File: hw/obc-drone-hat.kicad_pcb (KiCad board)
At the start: 4 copper layers, 65 x 56.5 mm, 68 parts, among them SW1 SW_DIP_x04

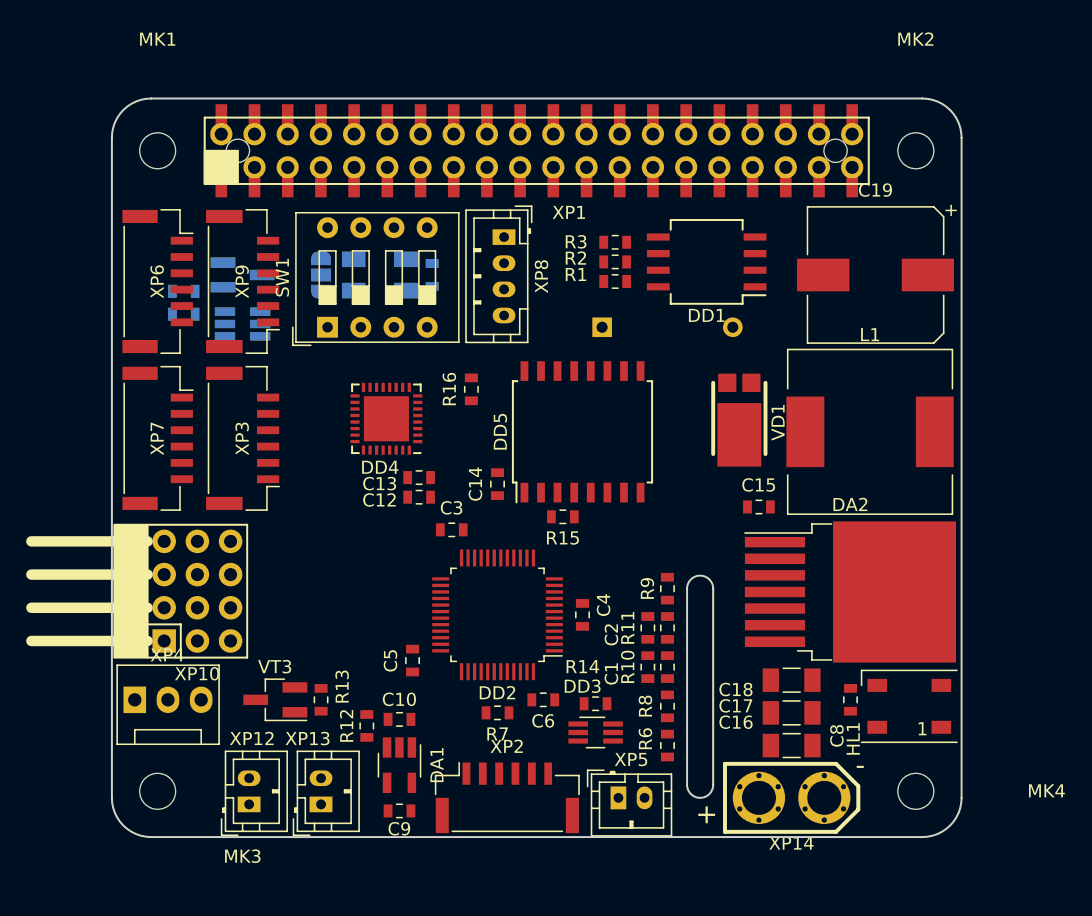
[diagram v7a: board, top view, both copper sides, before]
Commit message: hw: prepare to start wiring. add global GND planes
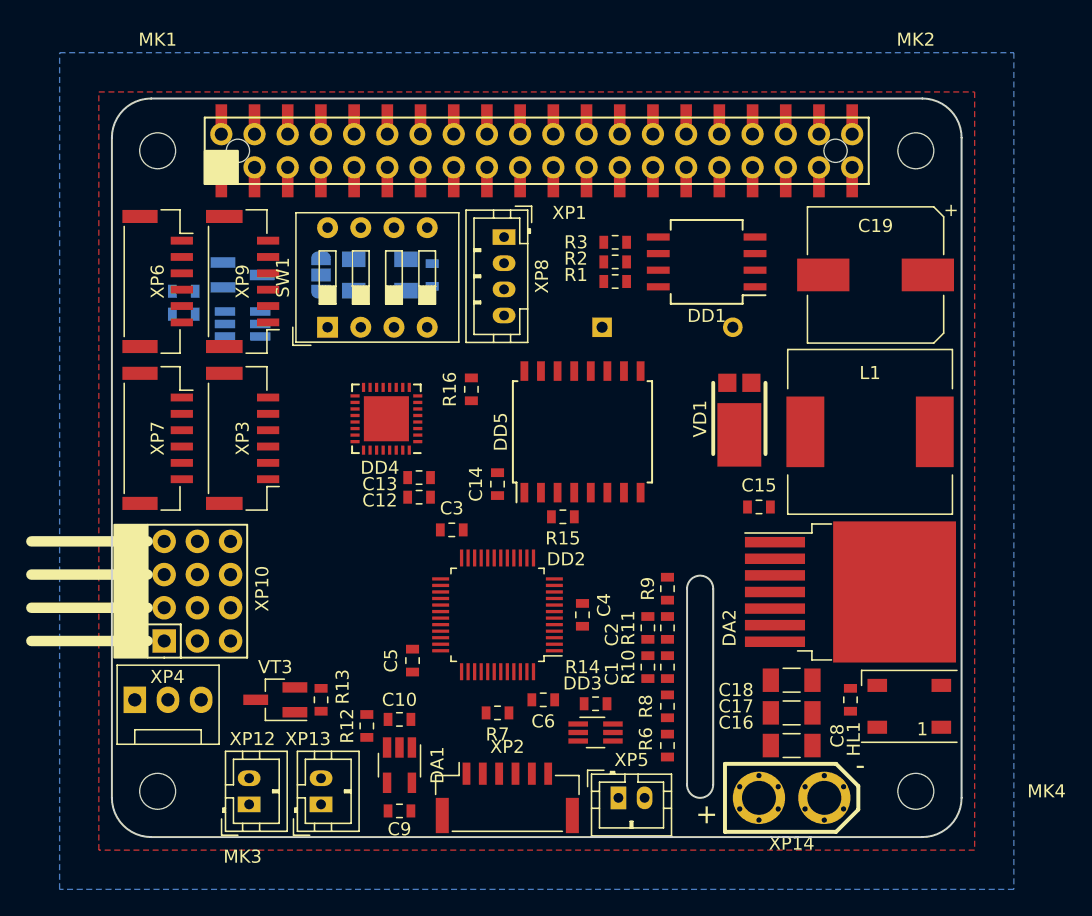
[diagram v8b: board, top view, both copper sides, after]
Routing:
- added copper zone on B.Cu, net GND
- added copper zone on F.Cu, net GND
- added copper zone on In1.Cu, net GND
- added copper zone on In2.Cu, net GND
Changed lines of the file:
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@@
     (aux_axis_origin 130 140)
     (grid_origin 130 140)
-    (visible_elements FFFFFF7F)
+    (visible_elements FFFFF77F)
     (pcbplotparams
       (layerselection 0x00030_80000001)
@@
     (descr "SMT capacitor, aluminium electrolytic, 10x10.5")
     (attr smd)
-    (fp_text reference C19 (at 0 6.46 180) (layer F.SilkS)
+    (fp_text reference C19 (at 0 3.75 180) (layer F.SilkS)
       (effects (font (size 1 1) (thickness 0.15)))
     )
@@
     (tags "D2PAK DDPAK TO-263 D2PAK-7 TO-263-7 SOT-427")
     (attr smd)
-    (fp_text reference DA2 (at 0 -6.65) (layer F.SilkS)
+    (fp_text reference DA2 (at -9.25 2.75 90) (layer F.SilkS)
       (effects (font (size 1 1) (thickness 0.15)))
     )
@@
     (tags "QFP 0.5")
     (attr smd)
-    (fp_text reference DD2 (at 0 -6 180) (layer F.SilkS)
+    (fp_text reference DD2 (at -5.25 4.25 180) (layer F.SilkS)
       (effects (font (size 1 1) (thickness 0.15)))
     )
@@
     (tags "SOT-363 SC-70-6 Handsoldering")
     (attr smd)
-    (fp_text reference DD3 (at -1 -3.5) (layer F.SilkS)
+    (fp_text reference DD3 (at -1 -3.75) (layer F.SilkS)
       (effects (font (size 1 1) (thickness 0.15)))
     )
@@
     (tags "Choke SMD")
     (attr smd)
-    (fp_text reference L1 (at 0 -7.4) (layer F.SilkS)
+    (fp_text reference L1 (at 0 -4.5) (layer F.SilkS)
       (effects (font (size 1 1) (thickness 0.15)))
     )
@@
     (descr "3-pin CPU fan Through hole pin header, see http://www.formfactors.org/developer%5Cspecs%5Crev1_2_public.pdf")
     (tags "pin header 3-pin CPU fan")
-    (fp_text reference XP4 (at 2.5 -3.4) (layer F.SilkS)
+    (fp_text reference XP4 (at 2.5 -1.75) (layer F.SilkS)
       (effects (font (size 1 1) (thickness 0.15)))
     )
@@
   (module hat:D-PowerDI-5 locked (layer F.Cu)
     (at 178 105.25 180)
-    (fp_text reference VD1 (at -3 -3 270) (layer F.SilkS)
+    (fp_text reference VD1 (at 3 -2.75 270) (layer F.SilkS)
       (effects (font (size 1 1) (thickness 0.15)))
     )
@@
   (module hat:SERVO4 locked (layer F.Cu)
     (at 134 125 90)
-    (fp_text reference XP10 (at -2.54 2.54 180) (layer F.SilkS)
+    (fp_text reference XP10 (at 4 7.5 270) (layer F.SilkS)
       (effects (font (size 1 1) (thickness 0.15)))
     )
@@
   (gr_line (start 130 86.5) (end 130 137) (layer Edge.Cuts) (width 0.15))
   (gr_line (start 133 83.5) (end 192 83.5) (layer Edge.Cuts) (width 0.15))
+  (zone (net 1) (net_name GND) (layer F.Cu) (hatch edge 0.508)
+    (connect_pads (clearance 0.508))
+    (min_thickness 0.254)
+    (fill yes (arc_segments 16) (thermal_gap 0.508) (thermal_bridge_width 0.508))
+    (polygon
+      (pts
+        (xy 129 83) (xy 196 83) (xy 196 141) (xy 129 141)
+      )
+    )
+  )
+  (zone (net 1) (net_name GND) (layer In1.Cu) (hatch edge 0.508)
+    (connect_pads (clearance 0.508))
+    (min_thickness 0.254)
+    (fill yes (arc_segments 16) (thermal_gap 0.508) (thermal_bridge_width 0.508))
+    (polygon
+      (pts
+        (xy 197 142) (xy 197 82) (xy 128 82) (xy 128 142)
+      )
+    )
+  )
+  (zone (net 1) (net_name GND) (layer In2.Cu) (hatch edge 0.508)
+    (connect_pads (clearance 0.508))
+    (min_thickness 0.254)
+    (fill yes (arc_segments 16) (thermal_gap 0.508) (thermal_bridge_width 0.508))
+    (polygon
+      (pts
+        (xy 127 81) (xy 198 81) (xy 198 143) (xy 127 143)
+      )
+    )
+  )
+  (zone (net 1) (net_name GND) (layer B.Cu) (hatch edge 0.508)
+    (connect_pads (clearance 0.508))
+    (min_thickness 0.254)
+    (fill yes (arc_segments 16) (thermal_gap 0.508) (thermal_bridge_width 0.508))
+    (polygon
+      (pts
+        (xy 126 80) (xy 199 80) (xy 199 144) (xy 126 144)
+      )
+    )
+  )
 )
